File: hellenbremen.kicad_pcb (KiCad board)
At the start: 4 copper layers, 102 x 107 mm, 32 parts, among them J2 Conn_01x03_Pin, J3 USB_C_Receptacle_USB2.0_16P, M1 Module-stlink-0.1, M2 Module-power_12and5V-0.2, M3 Module-mega-mcu144-0.6, M4 Module-vr-max9924-0.1, M5 Module-knock-0.2, U1 RNBD451PE-I100, U2 VNLD5160TR-E, U3 VNLD5160TR-E

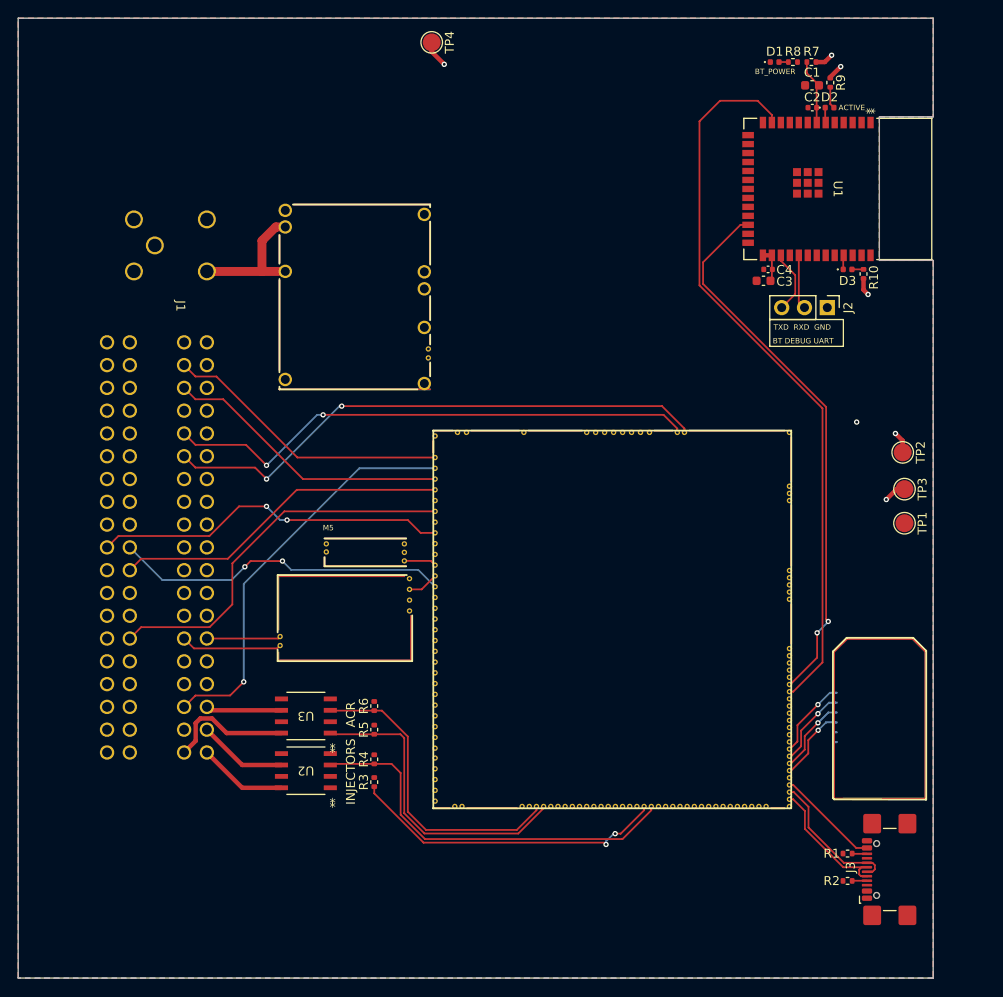
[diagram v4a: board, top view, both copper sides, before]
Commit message: igntion igbt, cooling mosfet
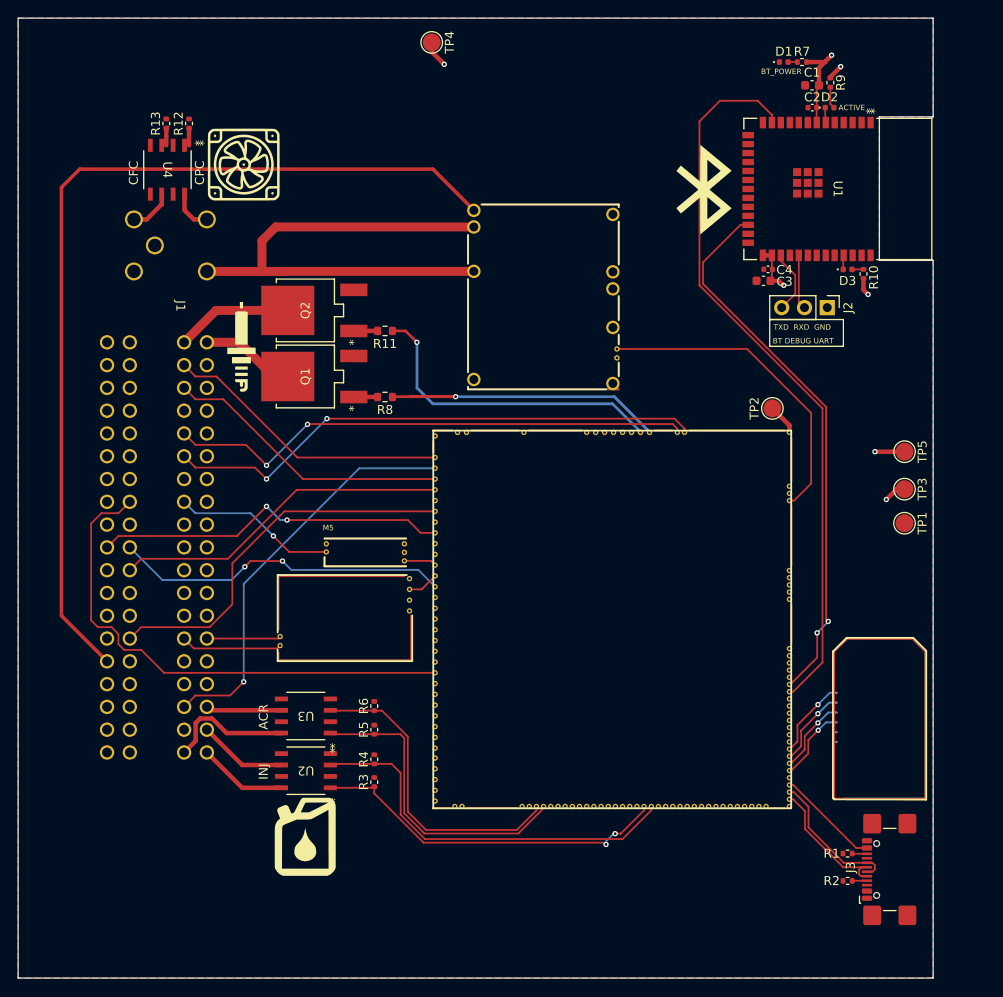
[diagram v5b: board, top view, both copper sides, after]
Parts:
- added G***: LOGO, hellen-bremen:cooling, F.Cu at (86.1, 51.3)
- added G***: LOGO, hellen-bremen:fuel, F.Cu at (93.0, 126.2)
- added G***: LOGO, hellen-bremen:ignition, F.Cu at (85.9, 71.6)
- added G***: LOGO, hellen-bremen:bluetooth, F.Cu at (137.4, 54.1)
- added Q1: ISL9V3040D3ST, ISL9V3040D3ST:TO-252AA_ONS, F.Cu at (93.0, 74.9)
- added Q2: ISL9V3040D3ST, ISL9V3040D3ST:TO-252AA_ONS, F.Cu at (93.0, 67.6)
- added R11: 22, Resistor_SMD:R_0603_1608Metric, F.Cu at (101.9, 69.8)
- added R12: 4.7k, Resistor_SMD:R_0402_1005Metric, F.Cu at (80.0, 46.7)
- added R13: 4.7k, Resistor_SMD:R_0402_1005Metric, F.Cu at (77.5, 46.7)
- added TP5: TestPoint_Probe, TestPoint:TestPoint_Pad_D2.0mm, F.Cu at (159.8, 83.3)
- added U4: VNLD5160TR-E, VNLD5160TR-E:SO_160TR-E_STM, F.Cu at (77.6, 51.9)
- R7: value 0 -> 470
- R8: value 470 -> 22; footprint Resistor_SMD:R_0402_1005Metric -> Resistor_SMD:R_0603_1608Metric
- moved R8 58.8 mm to (101.9, 77.2), turned to 180 degrees
- moved M2 21.0 mm to (111.0, 76.5)
- moved TP2 15.3 mm to (145.0, 78.5), turned to 90 degrees
- moved R7 1.05 mm to (148.3, 39.9)
- moved D1 1.02 mm to (146.3, 39.9)
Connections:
- C1 pad 2: 3V3_VDD_BT -> +3V3SW
- C2 pad 2: 3V3_VDD_BT -> +3V3SW
- C3 pad 2: 3V3_VDD_BT -> +3V3SW
- C4 pad 2: 3V3_VDD_BT -> +3V3SW
- J1 pad 1: unconnected-(J1-CFC-Pad1) -> CFC
- J1 pad 36: unconnected-(J1-FKSH-Pad36) -> RAW_KNOCK
- J1 pad 4: unconnected-(J1-CPC-Pad4) -> CPC
- J1 pad 55: unconnected-(J1-ETS-Pad55) -> ETS
- M3 pad E17: unconnected-(M3-OUT_PWM2-PadE17) -> MCU_CFC
- M3 pad E27: unconnected-(M3-OUT_PWM1-PadE27) -> MCU_CPC
- M3 pad S13: unconnected-(M3-IN_AUX1-PadS13) -> ETS
- M3 pad W10: IGN_2 -> MCUIGN_2
- M3 pad W11: IGN_1 -> MCUIGN_1
- R7 pad 1: 3V3_VDD_BT -> Net-(D1-A)
- R8 pad 1: Net-(D1-A) -> MCUIGN_1
- R8 pad 2: +3V3SW -> Net-(Q1-Pad1)
- U1 pad 27: 3V3_VDD_BT -> +3V3SW
- U1 pad 28: 3V3_VDD_BT -> +3V3SW
- U1 pad 7: 3V3_VDD_BT -> +3V3SW
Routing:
- net +12V_BAT: track 0.00 -> 103.7 mm
- net ETS: track 0.00 -> 57.5 mm
- net +12V_PSP: track 15.4 -> 57.4 mm
- net PWR_EN: track 0.00 -> 35.7 mm
- net MCUIGN_1: track 0.00 -> 35.4 mm, vias 0 -> 1
- net MCUIGN_2: track 0.00 -> 35.4 mm, vias 0 -> 1
- net RAW_KNOCK: track 0.00 -> 18.2 mm, vias 0 -> 1
- net +3V3SW: track 28.5 -> 43.3 mm, vias 4 -> 5
- net IGN_2: track 0.00 -> 13.0 mm
- net 3V3_VDD_BT: track 11.6 -> 0.00 mm
- net IGN_1: track 0.00 -> 10.6 mm
- net MCU_INJ1: track 35.4 -> 40.3 mm
- net CFC: track 0.00 -> 4.92 mm
- net CPC: track 0.00 -> 4.70 mm
- net Net-(Q2-Pad1): track 0.00 -> 2.59 mm
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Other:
- board text added: "CFC"
- board text added: "CPC"
- board text added: "INJ"
- board text removed: "INJECTORS"

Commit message: trying out a layout and routing
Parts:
- added G***: LOGO, hellen-bremen:logo, F.Cu at (111.0, 131.0)
- added G***: LOGO, hellen-bremen:qrcode, F.Cu at (136.0, 135.0)
- added M6: Module-knock-0.2, hellen_knock:knock, F.Cu at (86.2, 92.7)
- moved TP3 47.0 mm to (123.4, 57.7)
- moved R7 25.1 mm to (138.4, 63.0), turned to -90 degrees
- moved D1 22.5 mm to (138.4, 60.9), turned to -90 degrees
- moved TP4 22.5 mm to (123.2, 53.3)
- moved G*** 17.0 mm to (93.2, 109.2), turned to 90 degrees
- moved TP1 15.6 mm to (160.0, 75.7), turned to 0 degrees
- moved M2 13.1 mm to (102.4, 66.7)
- moved M5 12.3 mm to (86.2, 87.7)
- moved R5 11.3 mm to (95.8, 124.5), turned to -90 degrees
- moved R6 10.2 mm to (95.8, 120.7)
- moved TP2 9.86 mm to (139.4, 70.4)
- moved M3 9.61 mm to (103.0, 72.2)
- moved TP5 9.43 mm to (150.6, 85.6), turned to 0 degrees
- moved U3 9.34 mm to (91.5, 122.0)
- moved G*** 8.88 mm to (89.7, 43.2)
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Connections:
- net MCU_KNOCK renamed MCU_KNOCK_F
- net RAW_KNOCK renamed RAW_KNOCK_F
- J1 pad 14: unconnected-(J1-FHO2HG-Pad14) -> GND
- J1 pad 23: unconnected-(J1-RHO2HG-Pad23) -> GND
- J1 pad 26: unconnected-(J1-PCHO2SB1-Pad26) -> H2OSPC
- J1 pad 34: unconnected-(J1-JSS-Pad34) -> IN_JSS
- J1 pad 45: unconnected-(J1-RKSH-Pad45) -> RAW_KNOCK_R
- J1 pad 47: unconnected-(J1-FHO2SB1-Pad47) -> H2OS1
- J1 pad 48: unconnected-(J1-RHO2SB2-Pad48) -> H2OS2
- J1 pad 65: unconnected-(J1-PCH2OSG-Pad65) -> GND
- J1 pad 71: unconnected-(J1-AAT-Pad71) -> IN_AAT
- M2 pad V4: unconnected-(M2-5VP-PadV4) -> +5VP
- M3 pad E38: unconnected-(M3-V5A_SWITCHABLE-PadE38) -> +5VA
- M3 pad S11: unconnected-(M3-IN_AUX3-PadS11) -> H2OS1
- M3 pad S15: unconnected-(M3-IN_O2S2-PadS15) -> H2OS2
- M3 pad S16: unconnected-(M3-IN_O2S-PadS16) -> H2OS1
- M3 pad S17: unconnected-(M3-IN_RES1-PadS17) -> IN_JSS
- M3 pad S27: unconnected-(M3-IN_AT1-PadS27) -> IN_AAT
- M3 pad S9: unconnected-(M3-IN_SENS1-PadS9) -> MCU_KNOCK_R
- M3 pad W1: unconnected-(M3-GNDA-PadW1) -> GNDA
- M3 pad W2: unconnected-(M3-V5A_SWITCHABLE-PadW2) -> +5VA
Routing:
- net MCU_CFC: track 1.92 -> 124.6 mm, vias 0 -> 1
- net MCU_CPC: track 1.92 -> 111.1 mm, vias 0 -> 1
- net VIGN: track 0.00 -> 54.6 mm, vias 0 -> 2
- net IN_AAT: track 0.00 -> 54.6 mm
- net +3V3SW: track 43.3 -> 92.9 mm
- net H2OS2: track 0.00 -> 47.5 mm
- net H2OS1: track 0.00 -> 44.7 mm
- net +5V: track 3.95 -> 44.1 mm, vias 1 -> 0
- net RAW_KNOCK_R: track 0.00 -> 36.3 mm
- net IN_JSS: track 0.00 -> 29.6 mm, vias 0 -> 1
- net +12V_PSP: track 57.4 -> 37.1 mm
- net MCU_KNOCK_R: track 0.00 -> 18.6 mm, vias 0 -> 2
- net UART_BT_RX: track 61.4 -> 46.1 mm, vias 2 -> 0
- net CFC: track 4.92 -> 18.0 mm
- net UART_BT_TX: track 81.6 -> 69.1 mm, vias 0 -> 2
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- added copper zone on In2.Cu, net GND
- removed copper zone on In2.Cu, net +12V
- removed copper zone on In2.Cu, net +3V3SW
- removed copper zone on In2.Cu, net +5V
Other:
- board text added: "DON-PERFORMANCE.COM"
- board text added: "Hellen-Bremen rev. A"
- board text removed: "ACR"
- board text removed: "ACTIVE"
- board text removed: "BT_POWER"
- board text removed: "CFC"
- board text removed: "CPC"
- board text removed: "INJ"

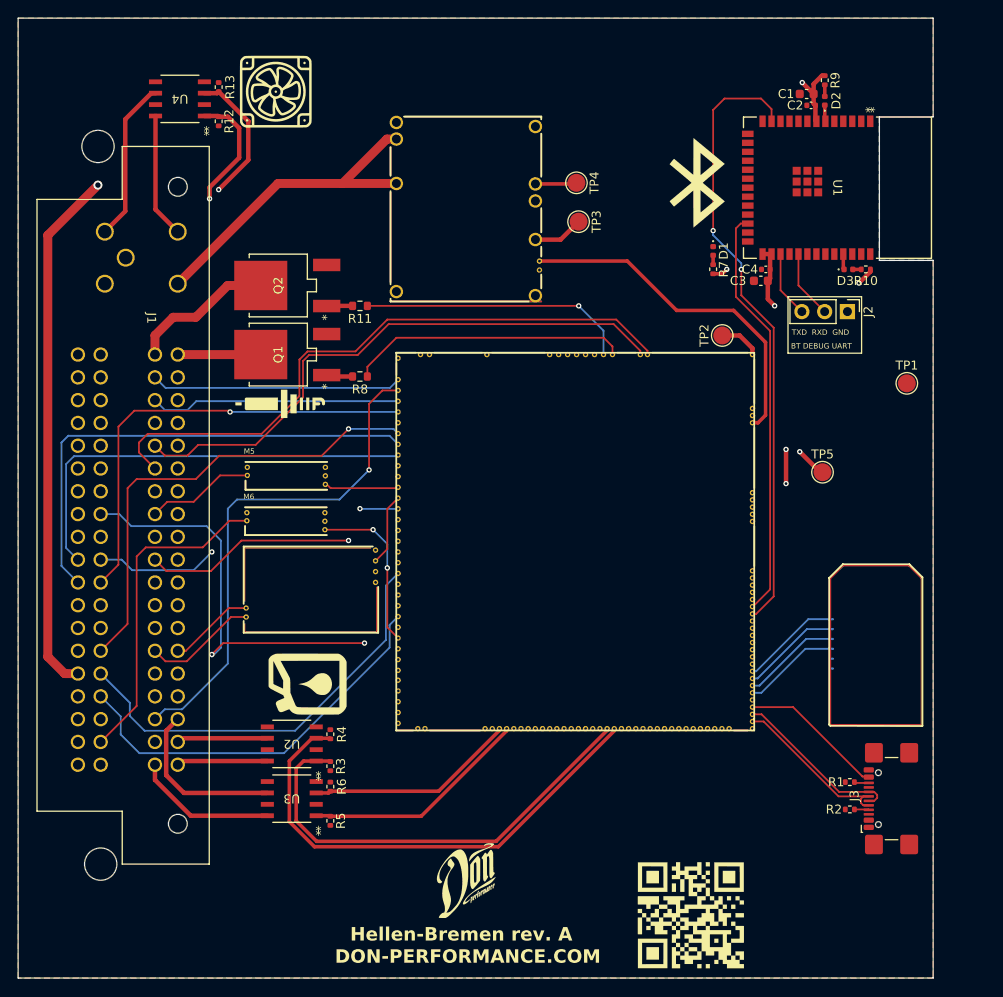
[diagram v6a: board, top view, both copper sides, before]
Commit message: more silkscreen pin markings, thicker power and ignition traces
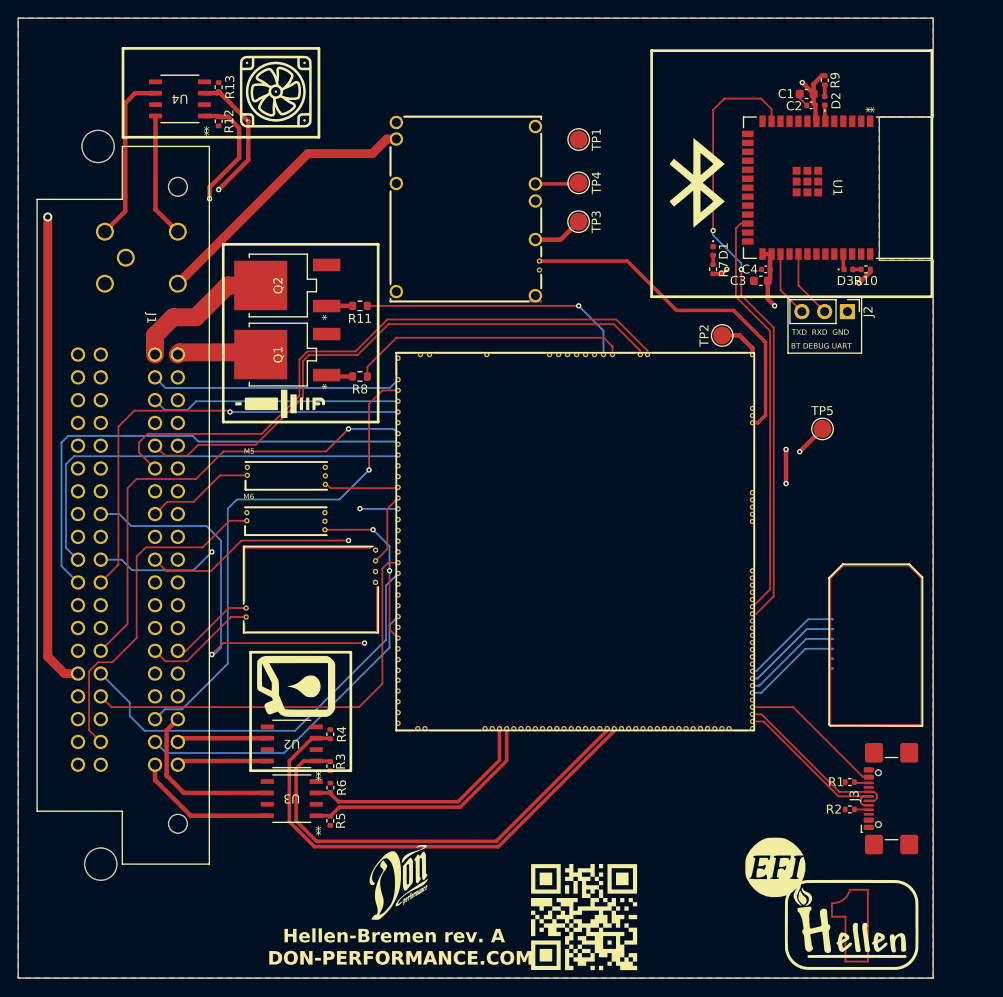
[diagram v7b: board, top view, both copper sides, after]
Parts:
- added G?: RUSEFI_LOGO, kicad6-libraries:rusefi_logo, F.Cu at (145.4, 129.7)
- added G?: LOGO, kicad6-libraries:LOGO, F.Cu at (154.2, 136.1)
- moved TP1 45.6 mm to (123.4, 48.5), turned to -90 degrees
- moved G*** 11.9 mm to (124.1, 135.2)
- moved G*** 7.50 mm to (103.5, 131.2)
- moved TP5 4.83 mm to (150.6, 80.8)
- moved G*** 1.30 mm to (91.9, 109.5)
- moved TP4 0.25 mm to (123.4, 53.3)
- moved R6 0.12 mm to (95.8, 120.8)
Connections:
- M2 pad V3: +12V_PSP -> +12V_BAT
- M3 pad S11: H2OS1 -> H2OSPC
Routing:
- net H2OSPC: track 0.00 -> 35.4 mm
- net +12V_BAT: track 95.2 -> 111.6 mm
- net +12V_PSP: track 37.1 -> 31.0 mm
- net H2OS1: track 44.7 -> 47.8 mm
- net MCU_ACR2: track 23.5 -> 26.3 mm
- net RAW_KNOCK_R: track 36.3 -> 38.3 mm
- net MCU_ACR1: track 25.4 -> 27.4 mm
- net GND: track 0.00 -> 1.60 mm
- net CFC: track 18.0 -> 19.1 mm

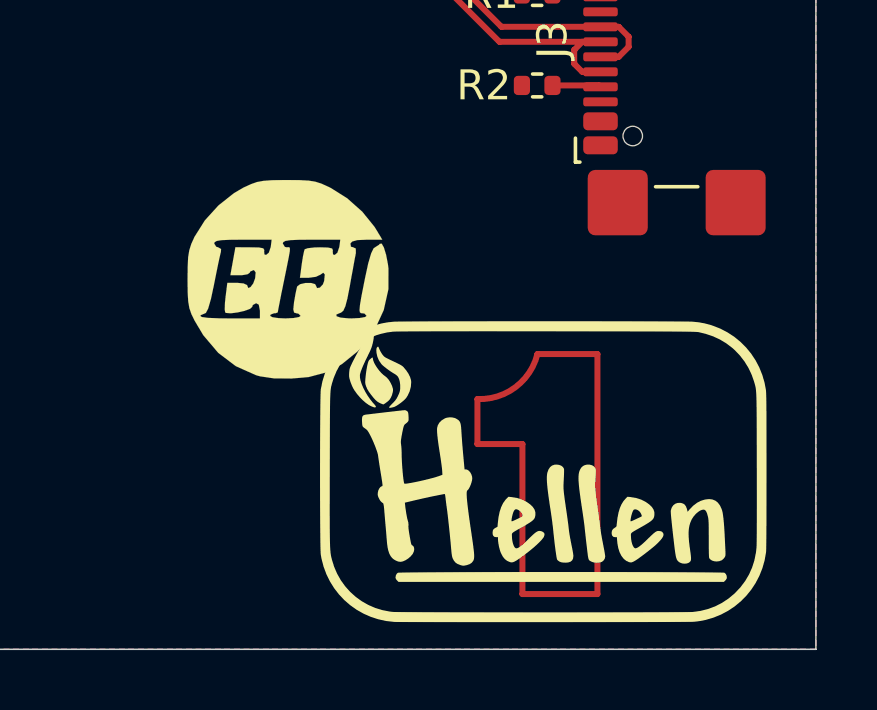
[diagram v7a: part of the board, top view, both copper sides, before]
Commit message: renaming graphics reference
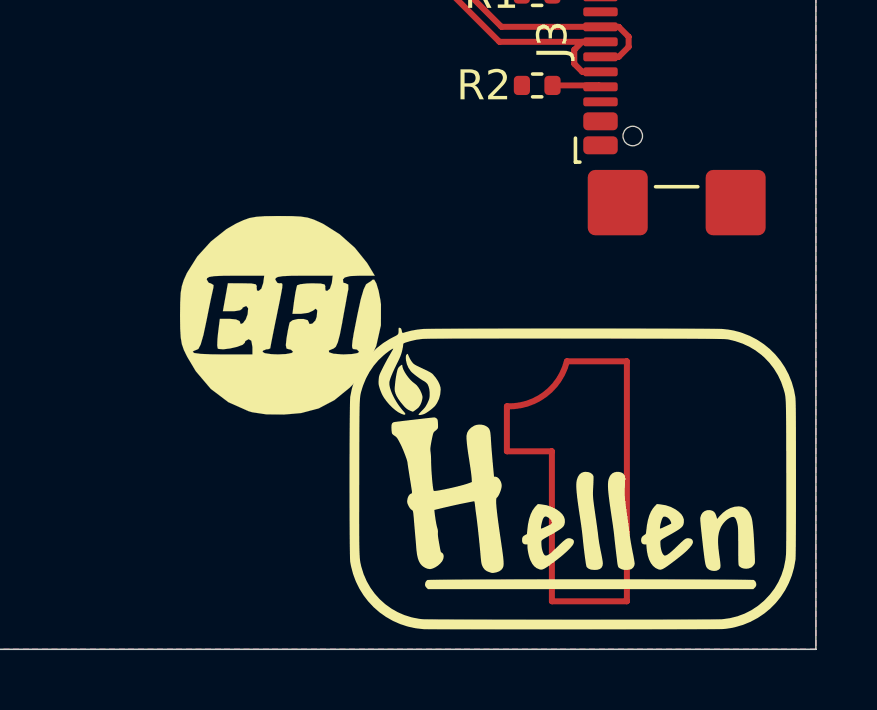
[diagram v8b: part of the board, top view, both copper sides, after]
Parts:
- removed G?: RUSEFI_LOGO, kicad6-libraries:rusefi_logo
- removed G?: LOGO, kicad6-libraries:LOGO
- added G1: RUSEFI_LOGO, kicad6-libraries:rusefi_logo, F.Cu at (145.1, 130.9)
- added G2: LOGO, kicad6-libraries:LOGO, F.Cu at (155.2, 136.4)
